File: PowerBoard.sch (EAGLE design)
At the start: 84 parts, among them IC1 MCP16311, IC2 MCP16311, IC3 DS2431P, U1 BQ24090, U2 MCP1726, U3 ATTINY85V, X2 MICROMATCH-4, X3 MICROMATCH-4

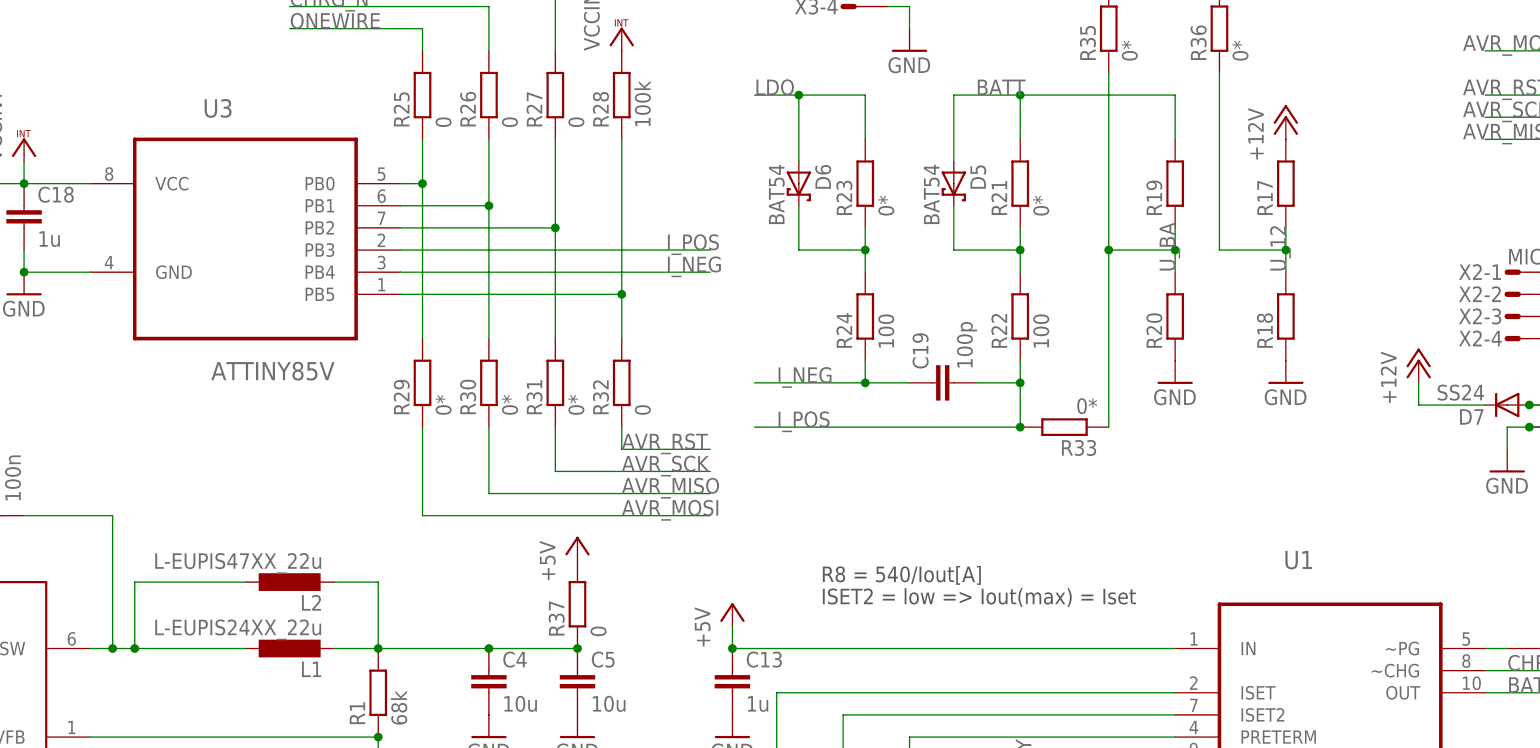
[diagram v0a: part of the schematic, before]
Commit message: Added all inputs from the bringup phase of Rev0
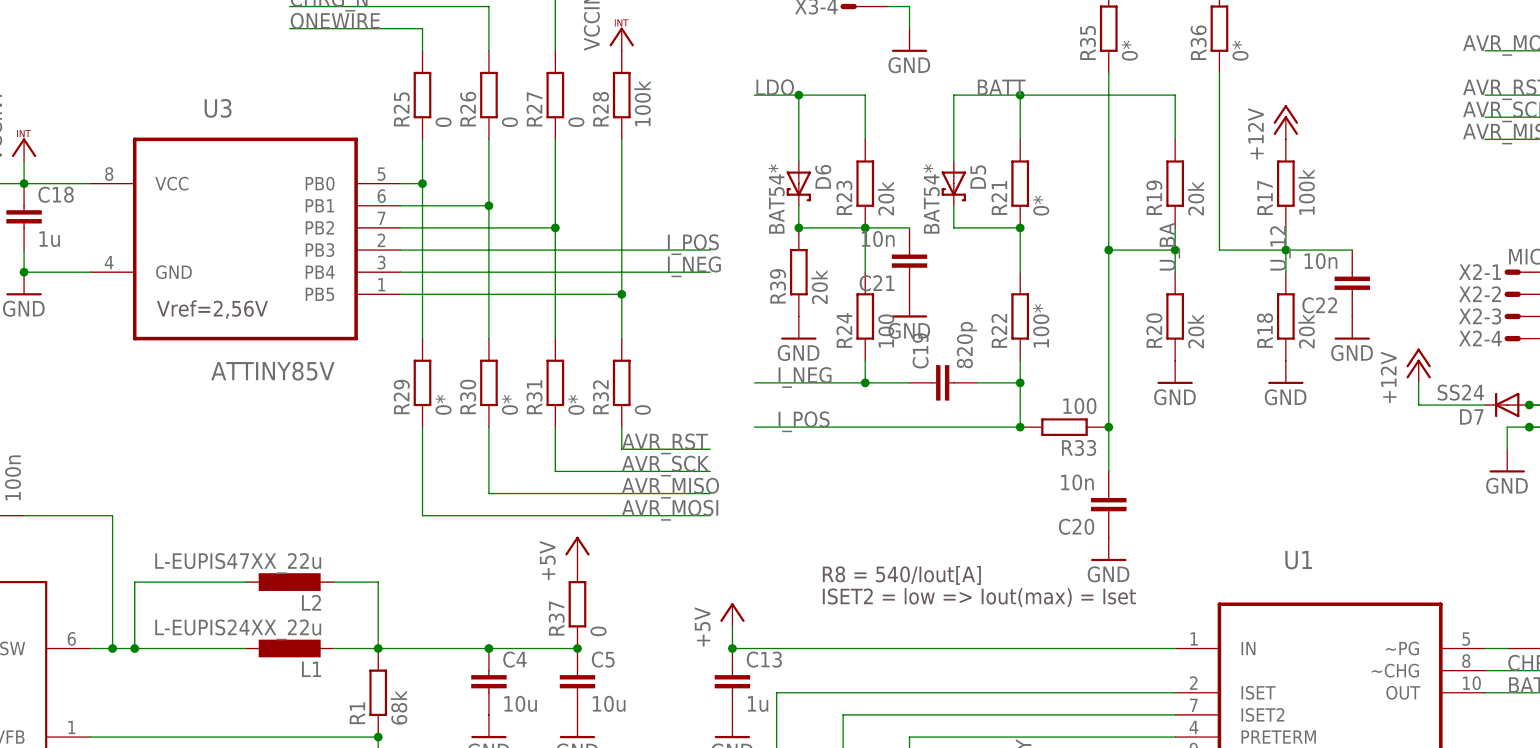
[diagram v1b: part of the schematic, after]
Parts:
- added C20, C21, C22: 10n, rcl:C-EUC0603
- added R39: 20k, rcl:R-EU_R0603
- C19: value 100p -> 820p
- D5, D6: value BAT54 -> BAT54*
- R17: value (none) -> 100k
- R18, R19, R20: value (none) -> 20k
- R22: value 100 -> 100*
- R23: value 0* -> 20k
- R33: value 0* -> 100
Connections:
- net GND: now also C20.1, C21.1, C22.1, R39.1
- net N$21: now also C21.2, R39.2
- net U_12: now also C22.2
- net U_BA: now also C20.2
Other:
- note added: "Vref=2,56V"
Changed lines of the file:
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@@
 <part name="VCC2" library="supply1" deviceset="VCCINT" device=""/>
 <part name="P+4" library="supply1" deviceset="+12V" device=""/>
-<part name="R17" library="rcl" deviceset="R-EU_" device="R0603"/>
-<part name="R18" library="rcl" deviceset="R-EU_" device="R0603"/>
+<part name="R17" library="rcl" deviceset="R-EU_" device="R0603" value="100k"/>
+<part name="R18" library="rcl" deviceset="R-EU_" device="R0603" value="20k"/>
 <part name="GND27" library="supply1" deviceset="GND" device=""/>
-<part name="R19" library="rcl" deviceset="R-EU_" device="R0603"/>
-<part name="R20" library="rcl" deviceset="R-EU_" device="R0603"/>
+<part name="R19" library="rcl" deviceset="R-EU_" device="R0603" value="20k"/>
+<part name="R20" library="rcl" deviceset="R-EU_" device="R0603" value="20k"/>
 <part name="GND28" library="supply1" deviceset="GND" device=""/>
-<part name="D5" library="diode" deviceset="BAT54" device=""/>
+<part name="D5" library="diode" deviceset="BAT54" device="" value="BAT54*"/>
 <part name="R21" library="rcl" deviceset="R-EU_" device="R0603" value="0*"/>
-<part name="R22" library="rcl" deviceset="R-EU_" device="R0603" value="100"/>
-<part name="C19" library="rcl" deviceset="C-EU" device="C0603" value="100p"/>
-<part name="R23" library="rcl" deviceset="R-EU_" device="R0603" value="0*"/>
-<part name="D6" library="diode" deviceset="BAT54" device=""/>
+<part name="R22" library="rcl" deviceset="R-EU_" device="R0603" value="100*"/>
+<part name="C19" library="rcl" deviceset="C-EU" device="C0603" value="820p"/>
+<part name="R23" library="rcl" deviceset="R-EU_" device="R0603" value="20k"/>
+<part name="D6" library="diode" deviceset="BAT54" device="" value="BAT54*"/>
 <part name="R24" library="rcl" deviceset="R-EU_" device="R0603" value="100"/>
 <part name="R25" library="rcl" deviceset="R-EU_" device="R0402" value="0"/>
@@
 <part name="R32" library="rcl" deviceset="R-EU_" device="R0402" value="0"/>
 <part name="VCC3" library="supply1" deviceset="VCCINT" device=""/>
-<part name="R33" library="rcl" deviceset="R-EU_" device="R0603" value="0*"/>
+<part name="R33" library="rcl" deviceset="R-EU_" device="R0603" value="100"/>
 <part name="JP2" library="pinhead" deviceset="PINHD-2X5" device=""/>
 <part name="X1" library="con-wago" deviceset="233-102" device=""/>
@@
 <part name="IC3" library="1wire" deviceset="DS2431" device="P"/>
 <part name="GND34" library="supply1" deviceset="GND" device=""/>
+<part name="R39" library="rcl" deviceset="R-EU_" device="R0603" value="20k"/>
+<part name="GND35" library="supply1" deviceset="GND" device=""/>
+<part name="C20" library="rcl" deviceset="C-EU" device="C0603" value="10n"/>
+<part name="C21" library="rcl" deviceset="C-EU" device="C0603" value="10n"/>
+<part name="GND36" library="supply1" deviceset="GND" device=""/>
+<part name="GND37" library="supply1" deviceset="GND" device=""/>
+<part name="C22" library="rcl" deviceset="C-EU" device="C0603" value="10n"/>
+<part name="GND38" library="supply1" deviceset="GND" device=""/>
 </parts>
 <sheets>
@@
 V+ &lt; +3V3</text>
 <text x="124.46" y="81.28" size="1.778" layer="97">ISET2 = low =&gt; Iout(max) = Iset</text>
+<text x="48.26" y="114.3" size="1.778" layer="97">Vref=2,56V</text>
 </plain>
 <instances>
@@
 <instance part="IC3" gate="_1W" x="243.84" y="116.84"/>
 <instance part="GND34" gate="1" x="248.92" y="106.68"/>
+<instance part="R39" gate="G$1" x="121.92" y="119.38" rot="R90"/>
+<instance part="GND35" gate="1" x="121.92" y="111.76"/>
+<instance part="C20" gate="G$1" x="157.48" y="91.44" rot="R180"/>
+<instance part="C21" gate="G$1" x="134.62" y="119.38" rot="R180"/>
+<instance part="GND36" gate="1" x="134.62" y="114.3"/>
+<instance part="GND37" gate="1" x="157.48" y="86.36"/>
+<instance part="C22" gate="G$1" x="185.42" y="116.84" rot="R180"/>
+<instance part="GND38" gate="1" x="185.42" y="111.76"/>
 </instances>
 <busses>
@@
 <pinref part="IC3" gate="P" pin="GND"/>
 <pinref part="GND34" gate="1" pin="GND"/>
+</segment>
+<segment>
+<pinref part="R39" gate="G$1" pin="1"/>
+<pinref part="GND35" gate="1" pin="GND"/>
+</segment>
+<segment>
+<pinref part="C21" gate="G$1" pin="1"/>
+<pinref part="GND36" gate="1" pin="GND"/>
+</segment>
+<segment>
+<pinref part="C20" gate="G$1" pin="1"/>
+<pinref part="GND37" gate="1" pin="GND"/>
+</segment>
+<segment>
+<pinref part="C22" gate="G$1" pin="1"/>
+<pinref part="GND38" gate="1" pin="GND"/>
 </segment>
 </net>
@@
 <wire x1="170.18" y1="121.92" x2="170.18" y2="142.24" width="0.1524" layer="91"/>
 <junction x="177.8" y="121.92"/>
+<pinref part="C22" gate="G$1" pin="2"/>
+<wire x1="185.42" y1="121.92" x2="177.8" y2="121.92" width="0.1524" layer="91"/>
 </segment>
 <segment>
@@
 <wire x1="157.48" y1="142.24" x2="157.48" y2="121.92" width="0.1524" layer="91"/>
 <junction x="157.48" y="121.92"/>
+<pinref part="C20" gate="G$1" pin="2"/>
+<wire x1="157.48" y1="96.52" x2="157.48" y2="101.6" width="0.1524" layer="91"/>
+<junction x="157.48" y="101.6"/>
 </segment>
 </net>
@@
 <segment>
 <pinref part="D5" gate="G$1" pin="C"/>
-<wire x1="139.7" y1="127" x2="139.7" y2="121.92" width="0.1524" layer="91"/>
-<wire x1="139.7" y1="121.92" x2="147.32" y2="121.92" width="0.1524" layer="91"/>
+<wire x1="139.7" y1="127" x2="139.7" y2="124.46" width="0.1524" layer="91"/>
+<wire x1="139.7" y1="124.46" x2="147.32" y2="124.46" width="0.1524" layer="91"/>
 <pinref part="R22" gate="G$1" pin="2"/>
-<wire x1="147.32" y1="119.38" x2="147.32" y2="121.92" width="0.1524" layer="91"/>
+<wire x1="147.32" y1="119.38" x2="147.32" y2="124.46" width="0.1524" layer="91"/>
 <pinref part="R21" gate="G$1" pin="1"/>
-<wire x1="147.32" y1="121.92" x2="147.32" y2="124.46" width="0.1524" layer="91"/>
-<junction x="147.32" y="121.92"/>
+<junction x="147.32" y="124.46"/>
 </segment>
 </net>
@@
 <pinref part="R24" gate="G$1" pin="2"/>
 <pinref part="R23" gate="G$1" pin="1"/>
-<wire x1="129.54" y1="119.38" x2="129.54" y2="121.92" width="0.1524" layer="91"/>
-<wire x1="129.54" y1="121.92" x2="129.54" y2="124.46" width="0.1524" layer="91"/>
-<wire x1="129.54" y1="121.92" x2="121.92" y2="121.92" width="0.1524" layer="91"/>
+<wire x1="129.54" y1="119.38" x2="129.54" y2="124.46" width="0.1524" layer="91"/>
+<wire x1="129.54" y1="124.46" x2="121.92" y2="124.46" width="0.1524" layer="91"/>
 <pinref part="D6" gate="G$1" pin="C"/>
-<wire x1="121.92" y1="121.92" x2="121.92" y2="127" width="0.1524" layer="91"/>
-<junction x="129.54" y="121.92"/>
-</segment>
-</net>
+<wire x1="121.92" y1="124.46" x2="121.92" y2="127" width="0.1524" layer="91"/>
+<junction x="129.54" y="124.46"/>
+<pinref part="R39" gate="G$1" pin="2"/>
+<junction x="121.92" y="124.46"/>
+<pinref part="C21" gate="G$1" pin="2"/>
+<wire x1="134.62" y1="124.46" x2="129.54" y2="124.46" width="0.1524" layer="91"/>
+</segment>
+</net>
